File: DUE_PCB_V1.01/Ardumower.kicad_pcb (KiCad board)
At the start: 2 copper layers, 169.3 x 95.5 mm, 99 parts, among them J1 I2C_1, J10 Bumper Left, J11 Bumper Right, J12 P_Left, J13 P_Right, J14 Sonar_R, J15 Sonar_C, J16 Sonar_L, J17 US1, J18 US2, J19 US3, J2 I2C_2, J20 Button, J21 5V IN, J22 Remote, J23 PCB_2, J24 3.3V IN, J25 TX0/RX0, J26 TX1/RX1, J27 TX2/RX2, J28 GPS_TX/GPS_RX, J29 Motor Left, J3 I2C_3, J30 Cutter Motor, J31 Motor Right, J32 Motor_Right1, J33 Motor_Right2, J34 Motor_Left1, J35 Motor_Left2, J36 Cutter_Motor, J37 ODORight1, J38 ODORight2, J39 ODOLeft1, J4 DS3231 RTC, J40 ODOLeft2, J41 ODOCutter, J5 9V IN, J6 Drop_Left, J7 Drop_Right, J8 Tilt, J9 Rain

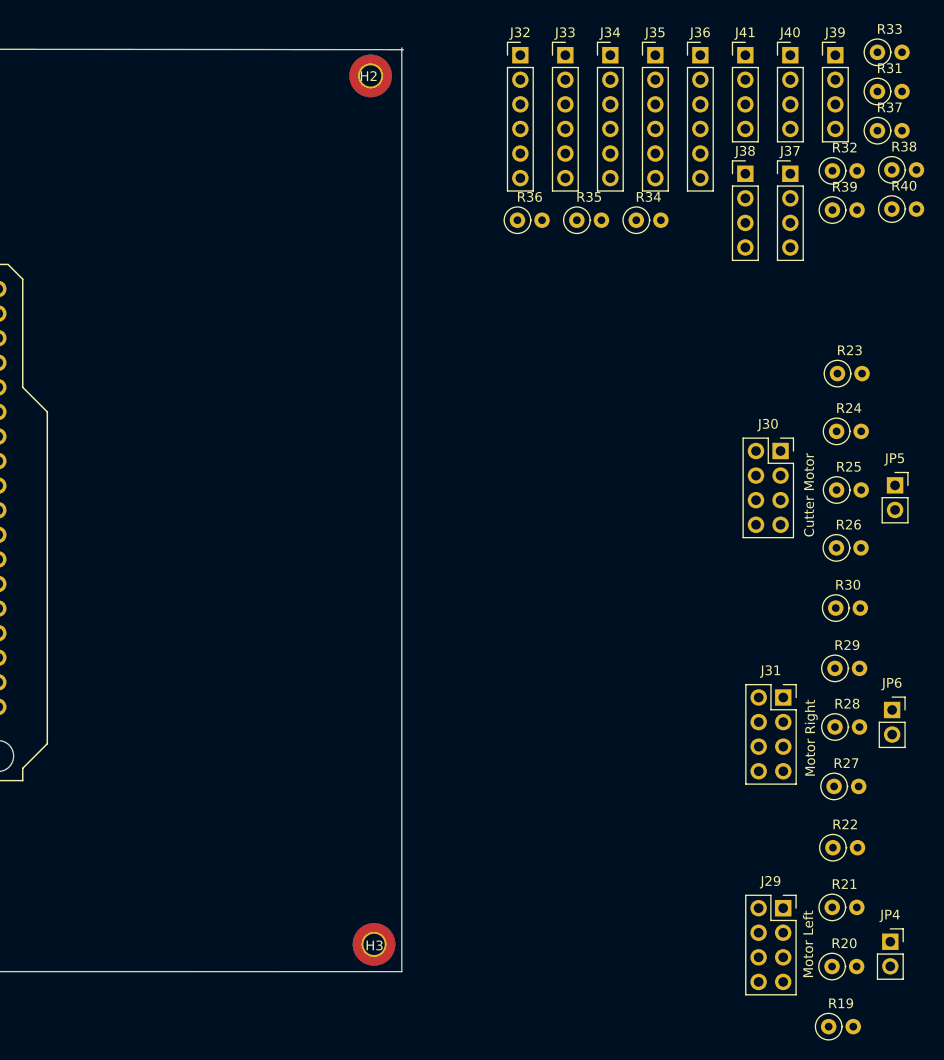
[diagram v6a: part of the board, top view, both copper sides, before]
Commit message: Add new Motor Schematic
Add new Motor Schematic
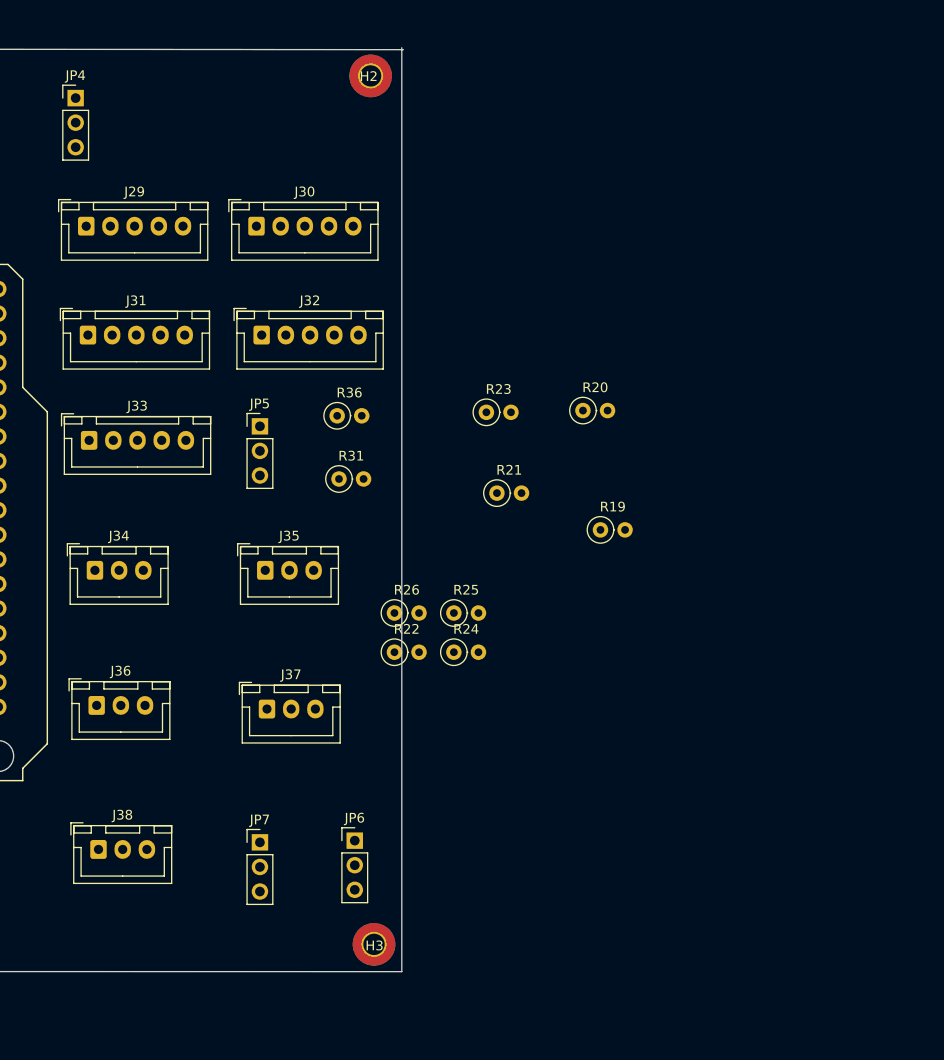
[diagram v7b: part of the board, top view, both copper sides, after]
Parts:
- removed J39: ODOLeft1, Connector_PinHeader_2.54mm:PinHeader_1x04_P2.54mm_Vertical
- removed J40: ODOLeft2, Connector_PinHeader_2.54mm:PinHeader_1x04_P2.54mm_Vertical
- removed J41: ODOCutter, Connector_PinHeader_2.54mm:PinHeader_1x04_P2.54mm_Vertical
- removed R27, R29, R37, R38, R39, R40: 1.5KO, Resistor_THT:R_Axial_DIN0207_L6.3mm_D2.5mm_P2.54mm_Vertical
- removed R28, R30, R32, R33, R34, R35: 1KO, Resistor_THT:R_Axial_DIN0207_L6.3mm_D2.5mm_P2.54mm_Vertical
- added JP7: CRPM_Power, Connector_PinHeader_2.54mm:PinHeader_1x03_P2.54mm_Vertical, F.Cu at (193.7, 117.6)
- J29: value Motor Left -> Motor_Right1; footprint Connector_PinSocket_2.54mm:PinSocket_2x04_P2.54mm_Vertical -> Connector_JST:JST_XH_B5B-XH-A_1x05_P2.50mm_Vertical
- J30: value Cutter Motor -> Motor_Right2; footprint Connector_PinSocket_2.54mm:PinSocket_2x04_P2.54mm_Vertical -> Connector_JST:JST_XH_B5B-XH-A_1x05_P2.50mm_Vertical
- J31: value Motor Right -> Motor_Left1; footprint Connector_PinSocket_2.54mm:PinSocket_2x04_P2.54mm_Vertical -> Connector_JST:JST_XH_B5B-XH-A_1x05_P2.50mm_Vertical
- J32: value Motor_Right1 -> Motor_Left2; footprint Connector_PinHeader_2.54mm:PinHeader_1x06_P2.54mm_Vertical -> Connector_JST:JST_XH_B5B-XH-A_1x05_P2.50mm_Vertical
- J33: value Motor_Right2 -> Cutter_Motor; footprint Connector_PinHeader_2.54mm:PinHeader_1x06_P2.54mm_Vertical -> Connector_JST:JST_XH_B5B-XH-A_1x05_P2.50mm_Vertical
- J34: value Motor_Left1 -> ODORight1; footprint Connector_PinHeader_2.54mm:PinHeader_1x06_P2.54mm_Vertical -> Connector_JST:JST_XH_B3B-XH-A_1x03_P2.50mm_Vertical
- J35: value Motor_Left2 -> ODORight2; footprint Connector_PinHeader_2.54mm:PinHeader_1x06_P2.54mm_Vertical -> Connector_JST:JST_XH_B3B-XH-A_1x03_P2.50mm_Vertical
- J36: value Cutter_Motor -> ODOLeft1; footprint Connector_PinHeader_2.54mm:PinHeader_1x06_P2.54mm_Vertical -> Connector_JST:JST_XH_B3B-XH-A_1x03_P2.50mm_Vertical
- J37: value ODORight1 -> ODOLeft2; footprint Connector_PinHeader_2.54mm:PinHeader_1x04_P2.54mm_Vertical -> Connector_JST:JST_XH_B3B-XH-A_1x03_P2.50mm_Vertical
- J38: value ODORight2 -> ODOCutter; footprint Connector_PinHeader_2.54mm:PinHeader_1x04_P2.54mm_Vertical -> Connector_JST:JST_XH_B3B-XH-A_1x03_P2.50mm_Vertical
- JP4: value 5V -> Motor_Driver_Power; footprint Connector_PinSocket_2.54mm:PinSocket_1x02_P2.54mm_Vertical -> Connector_PinHeader_2.54mm:PinHeader_1x03_P2.54mm_Vertical
- JP5: value 5V -> Cutter_Power; footprint Connector_PinSocket_2.54mm:PinSocket_1x02_P2.54mm_Vertical -> Connector_PinHeader_2.54mm:PinHeader_1x03_P2.54mm_Vertical
- JP6: value 5V -> ODO_Power; footprint Connector_PinSocket_2.54mm:PinSocket_1x02_P2.54mm_Vertical -> Connector_PinHeader_2.54mm:PinHeader_1x03_P2.54mm_Vertical
- R19, R21: value 1.5KO -> 1KO
- R24, R26: value 1KO -> 1.5KO
- moved JP4 121.2 mm to (174.6, 40.7)
- moved J29 100.8 mm to (175.7, 53.9)
- moved J38 96.7 mm to (177.0, 118.3)
- moved J36 91.7 mm to (176.8, 103.4)
- moved J31 81.0 mm to (175.9, 65.2)
- moved J37 77.4 mm to (194.4, 103.8)
- moved J34 75.3 mm to (176.6, 89.5)
- moved R31 68.5 mm to (201.8, 80.0)
- moved J35 66.8 mm to (194.2, 89.5)
- moved JP5 65.9 mm to (193.7, 74.6)
- moved J33 63.3 mm to (176.0, 76.0)
- moved R20 63.0 mm to (227.1, 73.0)
- moved J30 58.9 mm to (193.3, 53.9)
- moved JP6 57.1 mm to (203.5, 117.4)
- moved R19 56.5 mm to (228.9, 85.3)
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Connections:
- J29 pad 1: Net-(J29-Pad1) -> pinMotorRightPWM
- J29 pad 2: pinMotorEnable -> pinMotorRightDir
- J29 pad 3: pinMotorLeftDir -> pinMotorEnable
- J29 pad 5: MotorBreak -> GND
- J30 pad 1: Net-(J30-Pad1) -> pinMotorRight2PWM
- J30 pad 2: pinMotorMowEnable -> pinMotorRightDir
- J30 pad 3: pinMotorMowDir -> (no net)
- J30 pad 4: Net-(J30-Pad4) -> Net-(J29-Pad4)
- J30 pad 5: (no net) -> GND
- J31 pad 1: Net-(J31-Pad1) -> pinMotorLeftPWM
- J31 pad 2: pinMotorEnable -> pinMotorLeftDir
- J31 pad 3: pinMotorRightDir -> pinMotorEnable
- J31 pad 4: Net-(J31-Pad4) -> Net-(J29-Pad4)
- J31 pad 5: MotorBreak -> GND
- J32 pad 1: pinMotorRightPWM -> pinMotorLeft2PWM
- J32 pad 2: pinMotorRightDir -> pinMotorLeftDir
- J32 pad 3: pinMotorEnable -> (no net)
- J32 pad 4: +3V3 -> Net-(J29-Pad4)
- J32 pad 5: +5V -> GND
- J33 pad 1: pinMotorRight2PWM -> pinMotorMowPWM
- J33 pad 2: pinMotorRightDir -> pinMotorMowDir
- J33 pad 3: (no net) -> pinMotorMowEnable
- J33 pad 4: +3V3 -> Net-(J33-Pad4)
- J33 pad 5: +5V -> GND
- J34 pad 1: pinMotorLeftPWM -> Net-(J34-Pad1)
- J34 pad 2: pinMotorLeftDir -> Net-(J34-Pad2)
- J34 pad 3: pinMotorEnable -> GND
- J35 pad 1: pinMotorLeft2PWM -> Net-(J35-Pad1)
- J35 pad 2: pinMotorLeftDir -> Net-(J34-Pad2)
- J35 pad 3: (no net) -> GND
- J36 pad 1: pinMotorMowPWM -> Net-(J36-Pad1)
- J36 pad 2: pinMotorMowDir -> Net-(J34-Pad2)
- J36 pad 3: pinMotorMowEnable -> GND
- J37 pad 2: +3V3 -> Net-(J34-Pad2)
- J37 pad 3: +5V -> GND
- J38 pad 2: +3V3 -> Net-(J38-Pad2)
- J38 pad 3: +5V -> GND
- JP4 pad 1: +5VA -> +3V3
- JP4 pad 2: Net-(J29-Pad1) -> Net-(J29-Pad4)
- JP5 pad 1: +5VA -> +3V3
- JP5 pad 2: Net-(J30-Pad1) -> Net-(J33-Pad4)
- JP6 pad 1: +5VA -> +3V3
- JP6 pad 2: Net-(J31-Pad1) -> Net-(J34-Pad2)
- R19 pad 1: Net-(J29-Pad4) -> pinOdometryRight2
- R19 pad 2: GND -> Net-(J35-Pad1)
- R20 pad 1: Net-(J29-Pad4) -> pinOdometryLeft
- R20 pad 2: pinOdometryLeft -> Net-(J36-Pad1)
- R21 pad 1: Net-(J29-Pad6) -> pinOdometryLeft2
- R21 pad 2: GND -> Net-(J37-Pad1)
- R22 pad 1: Net-(J29-Pad6) -> pinMotorMowRpm
- R22 pad 2: pinMotorLeftFault -> Net-(J38-Pad1)
- R23 pad 1: Net-(J30-Pad4) -> Net-(J35-Pad1)
- R24 pad 1: Net-(J30-Pad4) -> Net-(J36-Pad1)
- R24 pad 2: pinMotorMowRpm -> GND
- R25 pad 1: Net-(J30-Pad6) -> Net-(J37-Pad1)
- R26 pad 1: Net-(J30-Pad6) -> Net-(J38-Pad1)
- R26 pad 2: pinMotorMowFault -> GND
- R31 pad 2: Net-(J37-Pad1) -> Net-(J34-Pad1)
- R36 pad 1: Net-(J37-Pad1) -> Net-(J34-Pad1)
- XA1 pad D25: pinMotorLeftFault -> (no net)
- XA1 pad D26: pinMotorMowFault -> (no net)
- XA1 pad D27: pinMotorRightFault -> (no net)

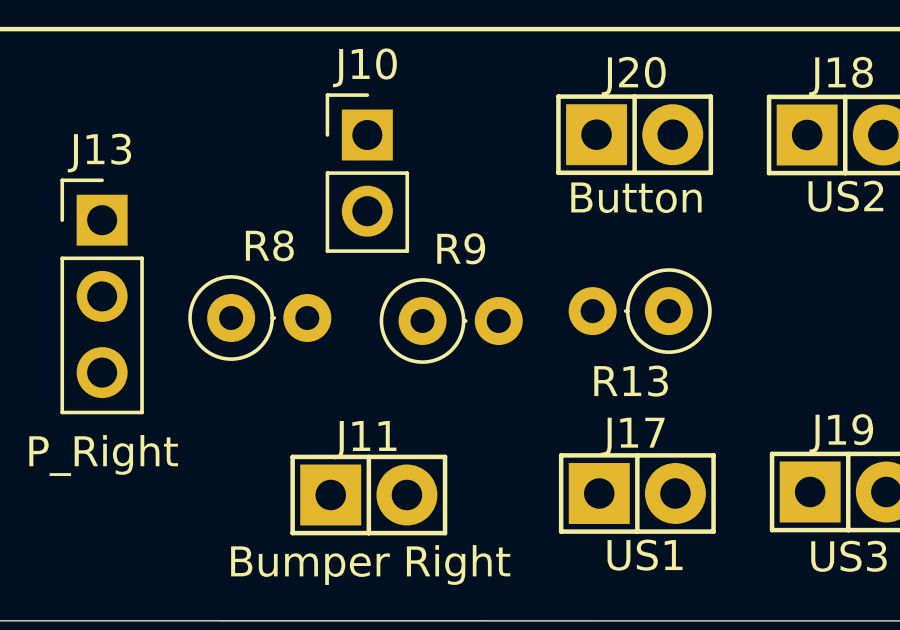
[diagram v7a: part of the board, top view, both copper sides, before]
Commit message: Rename Pins
Rename ReservePinA10 to pinMotorLeftSense2
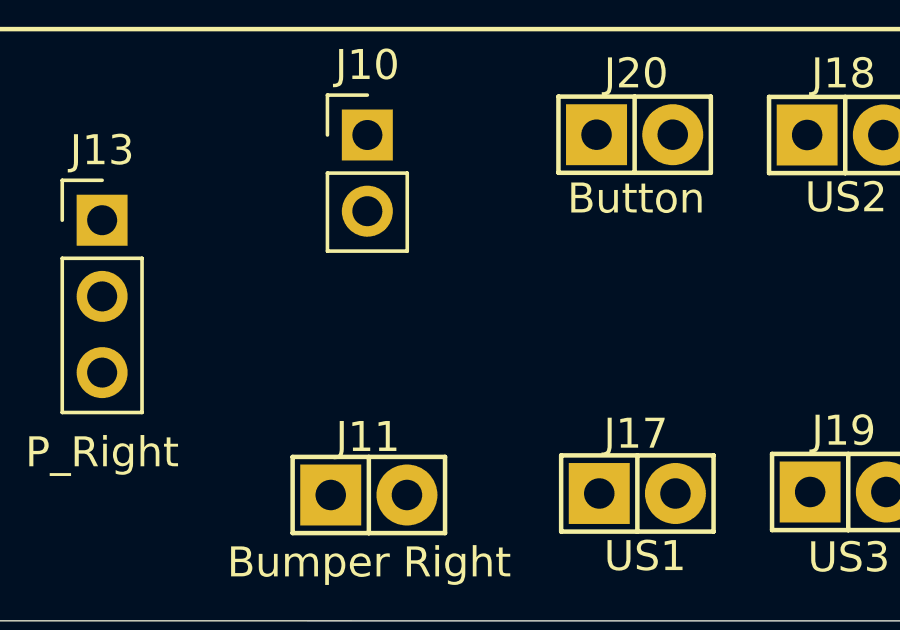
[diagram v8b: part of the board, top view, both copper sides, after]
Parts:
- removed R13, R8, R9: 10k, Resistor_THT:R_Axial_DIN0207_L6.3mm_D2.5mm_P2.54mm_Vertical
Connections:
- J30 pad 3: (no net) -> pinMotorEnable
- J32 pad 3: (no net) -> pinMotorEnable
- XA1 pad IORF: IOREV -> (no net)
